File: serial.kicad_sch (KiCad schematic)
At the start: 28 parts, among them U13 4069, U14 LM348DR, X2 1.8432MHz

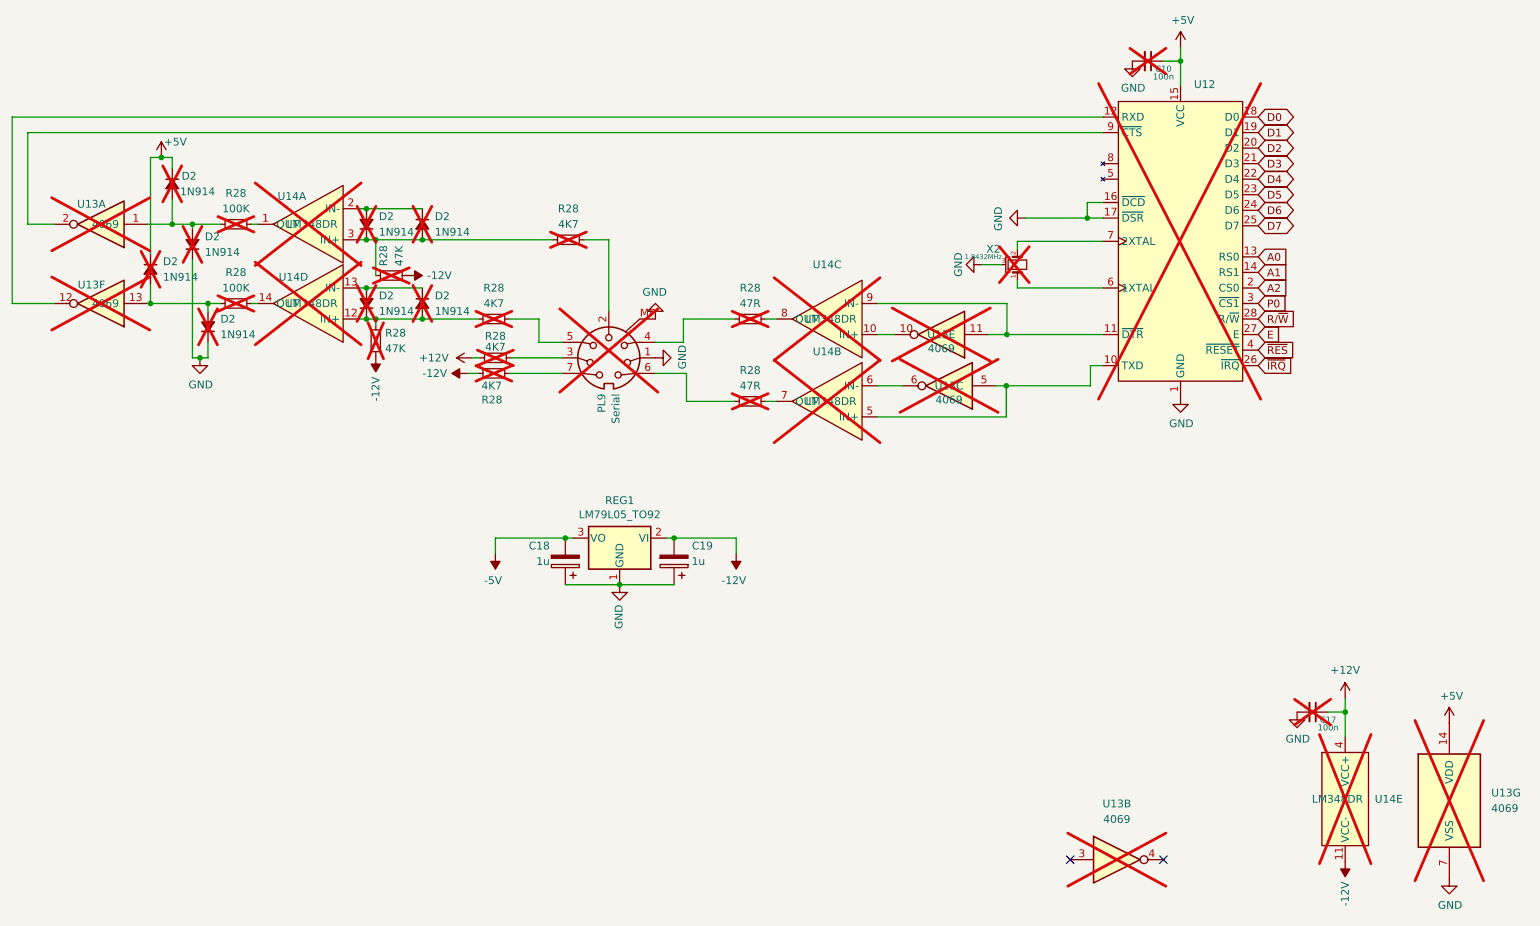
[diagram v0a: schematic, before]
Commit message: add uart to board
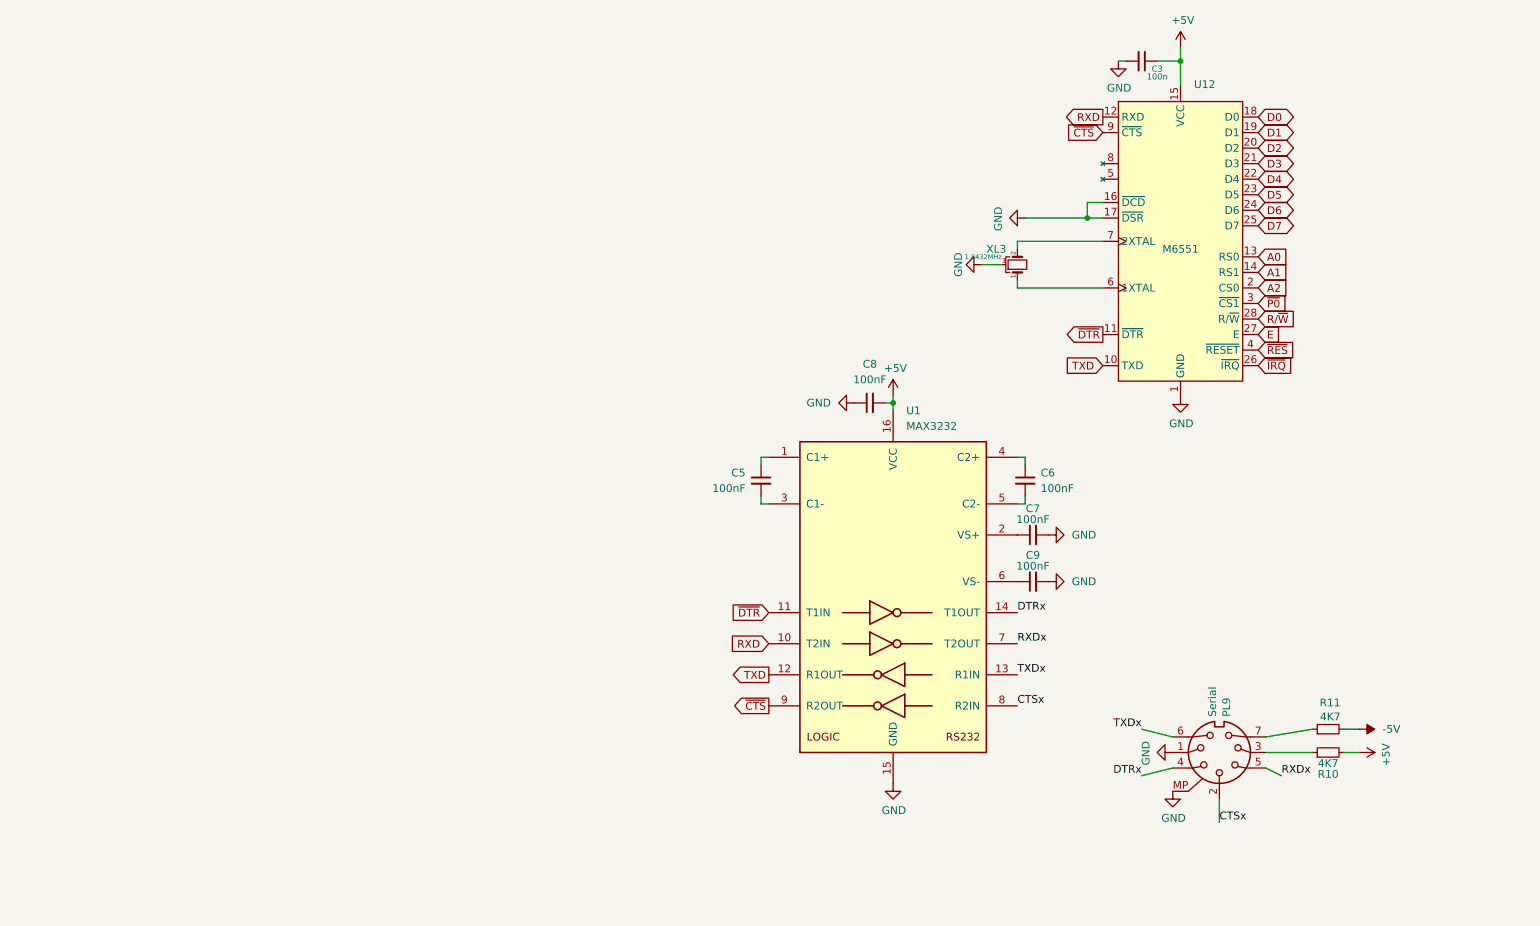
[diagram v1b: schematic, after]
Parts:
- removed C10, C17: 100n, Capacitor_SMD:C_0805_2012Metric_Pad1.18x1.45mm_HandSolder, symbol Device:C_Small
- removed C18, C19: 1u, Capacitor_Tantalum_SMD:CP_EIA-3216-18_Kemet-A_Pad1.58x1.35mm_HandSolder, symbol Device:C_Polarized
- removed D2 (x8): 1N914, Diode_SMD:D_SOD-323_HandSoldering, symbol Device:D_Small_Filled
- removed R28 (x2): 47K, Resistor_SMD:R_0805_2012Metric_Pad1.20x1.40mm_HandSolder, symbol Device:R_Small
- removed R28 (x4): 4K7, Resistor_SMD:R_0805_2012Metric_Pad1.20x1.40mm_HandSolder, symbol Device:R_Small
- removed R28 (x2): 100K, Resistor_SMD:R_0805_2012Metric_Pad1.20x1.40mm_HandSolder, symbol Device:R_Small
- removed R28 (x2): 47R, Resistor_SMD:R_0805_2012Metric_Pad1.20x1.40mm_HandSolder, symbol Device:R_Small
- removed REG1: LM79L05_TO92, Package_TO_SOT_SMD:SOT-89-3_Handsoldering, symbol Regulator_Linear:LM79L05_TO92
- removed U13: 4069, Package_SO:SOIC-14_3.9x8.7mm_P1.27mm, symbol 4xxx:4069
- removed U14: LM348DR, Package_SO:SOIC-14_3.9x8.7mm_P1.27mm, symbol Motorola PIA:LM348x
- added C3: 100n, Capacitor_SMD:C_0805_2012Metric_Pad1.18x1.45mm_HandSolder, symbol Device:C_Small
- added C5, C6, C7, C8, C9: 100nF, Capacitor_SMD:C_0805_2012Metric_Pad1.18x1.45mm_HandSolder, symbol Device:C_Small
- added R10, R11: 4K7, Resistor_SMD:R_0805_2012Metric_Pad1.20x1.40mm_HandSolder, symbol Device:R_Small
- added U1: MAX3232, Package_DIP:DIP-16_W7.62mm, symbol Interface_UART:MAX3232
- PL9: now fitted
- U12: value ~ -> M6551; now fitted
- XL3: renamed from X2; now fitted
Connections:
- net +5V: now also C3.1, C8.2, R10.2, U1.16 (VCC)
- net -5V: now also R11.2
- net GND: now also C3.2, C7.2, C8.1, C9.2, U1.15 (GND)
- net TXD: now reaches U12.10 (TXD)
- net TXD: now also U1.12 (R1OUT)
- net at PL9.7: now also R11.1
- net RXDx: now reaches PL9.5
- net RXDx: now also U1.7 (T2OUT)
- net ~{DTR}: now reaches U12.11 (~{DTR})
- net ~{DTR}: now also U1.11 (T1IN)
- net RXD: now reaches U12.12 (RXD)
- net RXD: now also U1.10 (T2IN)
- net ~{CTS}: now reaches U12.9 (~{CTS})
- net ~{CTS}: now also U1.9 (R2OUT)
- net at PL9.3: now also R10.1
- net TXDx: now reaches PL9.6
- net TXDx: now also U1.13 (R1IN)
- net DTRx: now reaches PL9.4
- net DTRx: now also U1.14 (T1OUT)
- net CTSx: now reaches PL9.2
- net CTSx: now also U1.8 (R2IN)
- net P0 renamed ~{P0}
- new net: C5.1, U1.1 (C1+)
- new net: C7.1, U1.2 (VS+)
- new net: C5.2, U1.3 (C1-)
- new net: C6.1, U1.4 (C2+)
- new net: C6.2, U1.5 (C2-)
- new net: C9.1, U1.6 (VS-)
- no-connect marks 2 -> 0

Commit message: refresh BOM
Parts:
- C3: value 100n -> 100nF; footprint Capacitor_SMD:C_0805_2012Metric_Pad1.18x1.45mm_HandSolder -> PCM_Capacitor_SMD_AKL:C_0805_2012Metric_Pad1.18x1.45mm_HandSolder; LCSC (none) -> C1711
- C5, C6, C7, C8, C9: footprint Capacitor_SMD:C_0805_2012Metric_Pad1.18x1.45mm_HandSolder -> PCM_Capacitor_SMD_AKL:C_0805_2012Metric_Pad1.18x1.45mm_HandSolder; DigiKey 311-1140-1-ND -> (none); LCSC MBK0805X7R104K500NT -> C1711
- R10, R11: LCSC (none) -> C17673
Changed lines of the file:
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@@
+			)
+		)
+		(property "LCSC" "C17673"
+			(at 250.19 133.35 90)
+			(effects
+				(font
+					(size 1.27 1.27)
+				)
+				(hide yes)
 			)
 		)
@@
 			)
 		)
-		(property "Footprint" "Capacitor_SMD:C_0805_2012Metric_Pad1.18x1.45mm_HandSolder"
+		(property "Footprint" "PCM_Capacitor_SMD_AKL:C_0805_2012Metric_Pad1.18x1.45mm_HandSolder"
 			(at 201.93 109.22 0)
 			(effects
@@
 			)
 		)
-		(property "DigiKey" "311-1140-1-ND"
+		(property "DigiKey" ""
 			(at 201.93 109.22 0)
 			(effects
@@
 			)
 		)
-		(property "LCSC" "MBK0805X7R104K500NT"
+		(property "LCSC" "C1711"
 			(at 201.93 109.22 0)
 			(effects
@@
 			)
 		)
-		(property "Footprint" "Capacitor_SMD:C_0805_2012Metric_Pad1.18x1.45mm_HandSolder"
+		(property "Footprint" "PCM_Capacitor_SMD_AKL:C_0805_2012Metric_Pad1.18x1.45mm_HandSolder"
 			(at 175.26 80.01 0)
 			(effects
@@
 			)
 		)
-		(property "DigiKey" "311-1140-1-ND"
+		(property "DigiKey" ""
 			(at 175.26 80.01 0)
 			(effects
@@
 			)
 		)
-		(property "LCSC" "MBK0805X7R104K500NT"
+		(property "LCSC" "C1711"
 			(at 175.26 80.01 0)
 			(effects
@@
 			)
 		)
-		(property "Footprint" "Capacitor_SMD:C_0805_2012Metric_Pad1.18x1.45mm_HandSolder"
+		(property "Footprint" "PCM_Capacitor_SMD_AKL:C_0805_2012Metric_Pad1.18x1.45mm_HandSolder"
 			(at 157.48 92.71 0)
 			(effects
@@
 			)
 		)
-		(property "DigiKey" "311-1140-1-ND"
+		(property "DigiKey" ""
 			(at 157.48 92.71 0)
 			(effects
@@
 			)
 		)
-		(property "LCSC" "MBK0805X7R104K500NT"
+		(property "LCSC" "C1711"
 			(at 157.48 92.71 0)
 			(effects
@@
 			)
 		)
-		(property "Value" "100n"
+		(property "Value" "100nF"
 			(at 222.25 26.67 90)
 			(effects
@@
 			)
 		)
-		(property "Footprint" "Capacitor_SMD:C_0805_2012Metric_Pad1.18x1.45mm_HandSolder"
+		(property "Footprint" "PCM_Capacitor_SMD_AKL:C_0805_2012Metric_Pad1.18x1.45mm_HandSolder"
 			(at 219.71 24.13 0)
 			(effects
@@
 			)
 		)
+		(property "LCSC" "C1711"
+			(at 219.71 24.13 90)
+			(effects
+				(font
+					(size 1.27 1.27)
+				)
+				(hide yes)
+			)
+		)
 		(pin "1"
 		)
@@
 			)
 		)
-		(property "Footprint" "Capacitor_SMD:C_0805_2012Metric_Pad1.18x1.45mm_HandSolder"
+		(property "Footprint" "PCM_Capacitor_SMD_AKL:C_0805_2012Metric_Pad1.18x1.45mm_HandSolder"
 			(at 201.93 101.6 0)
 			(effects
@@
 			)
 		)
-		(property "DigiKey" "311-1140-1-ND"
+		(property "DigiKey" ""
 			(at 201.93 101.6 0)
 			(effects
@@
 			)
 		)
-		(property "LCSC" "MBK0805X7R104K500NT"
+		(property "LCSC" "C1711"
 			(at 201.93 101.6 0)
 			(effects
@@
 			)
 		)
+		(property "LCSC" "C17673"
+			(at 250.19 137.16 90)
+			(effects
+				(font
+					(size 1.27 1.27)
+				)
+				(hide yes)
+			)
+		)
 		(pin "1"
 		)
@@
 			)
 		)
-		(property "Footprint" "Capacitor_SMD:C_0805_2012Metric_Pad1.18x1.45mm_HandSolder"
+		(property "Footprint" "PCM_Capacitor_SMD_AKL:C_0805_2012Metric_Pad1.18x1.45mm_HandSolder"
 			(at 200.66 92.71 0)
 			(effects
@@
 			)
 		)
-		(property "DigiKey" "311-1140-1-ND"
+		(property "DigiKey" ""
 			(at 200.66 92.71 0)
 			(effects
@@
 			)
 		)
-		(property "LCSC" "MBK0805X7R104K500NT"
+		(property "LCSC" "C1711"
 			(at 200.66 92.71 0)
 			(effects

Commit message: align versions
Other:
- title: (none) -> Dragon CPU UK Revised
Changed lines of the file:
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@@
 	(generator_version "9.0")
 	(paper "A4")
+	(title_block
+		(title "Dragon CPU UK Revised")
+		(date "2025-10-05")
+		(rev "3.3")
+		(comment 1 "Redesign by Julian Brown")
+	)
 	(junction
 		(at 226.06 24.13)
